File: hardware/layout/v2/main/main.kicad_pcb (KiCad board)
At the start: 4 copper layers, 31.5 x 76.5 mm, 52 parts, among them J1 KNX bus terminal pins, J2 AUX, J3 DALI, J4 Controller cable, J5 Interface DALI, J6 Interface logic, Q1 MJD45H11, Q2 BC857, U1 NCN5130MNTWG, U2 SCT2400TVBR, U3 REM3-2415S/A/CTRL 24V->15V 3W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, U4 TLP383, Y1 16MHz

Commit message: Updated DALI DC-DC converter from RECOM REM3-2415S/A to REC3-2415SRW/H2/A series across all variants, changed V3 OLED from 14-pin 0.5mm ZIF to 14-pin 0.62mm solder-tail FPC connector, and expanded assembly documentation with Mouser/Digi-Key/TME part numbers and alternative suppliers
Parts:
- U3: value REM3-2415S/A/CTRL 24V->15V 3W iso -> REC3-2415SRW/H2/A/CTRL 24V->15V 3W iso

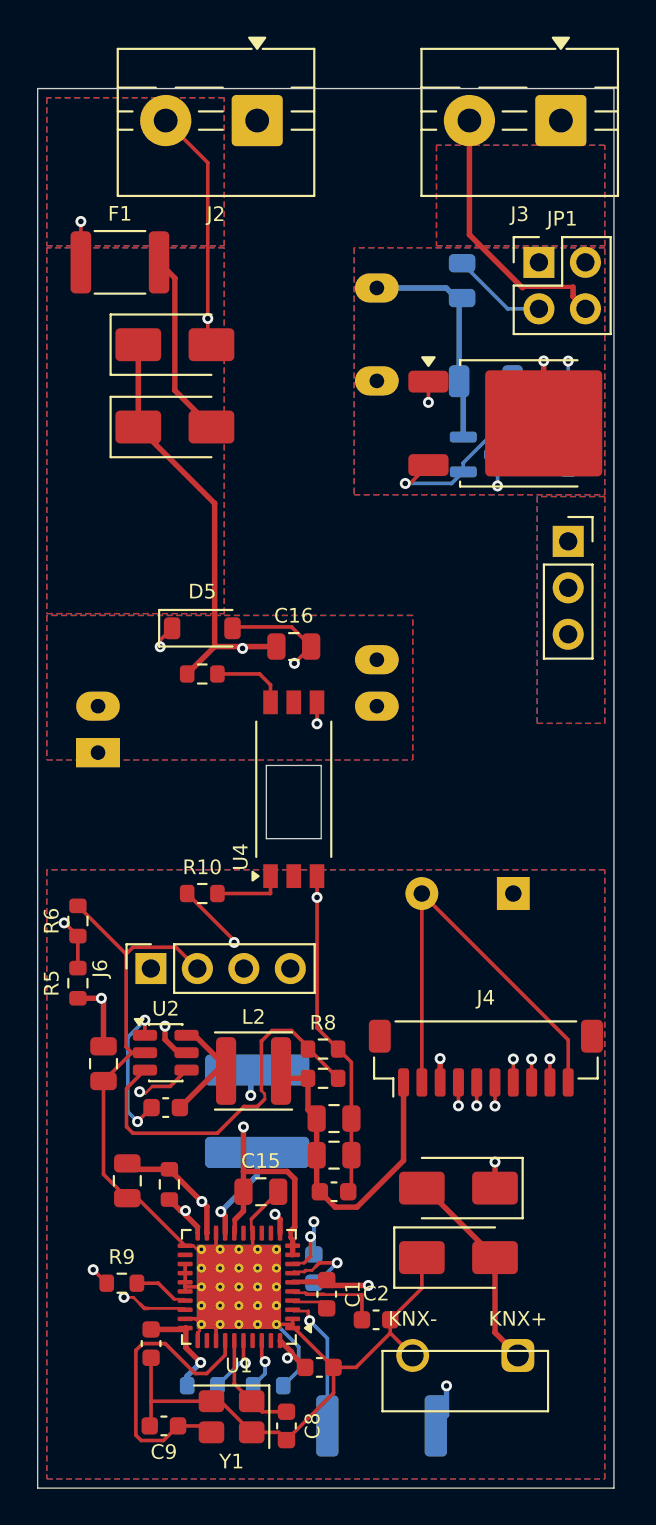
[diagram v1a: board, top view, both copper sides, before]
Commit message: Removed V1 hardware variant from CI workflows, updated AGENTS.md documentation to reflect V2/V3-only support
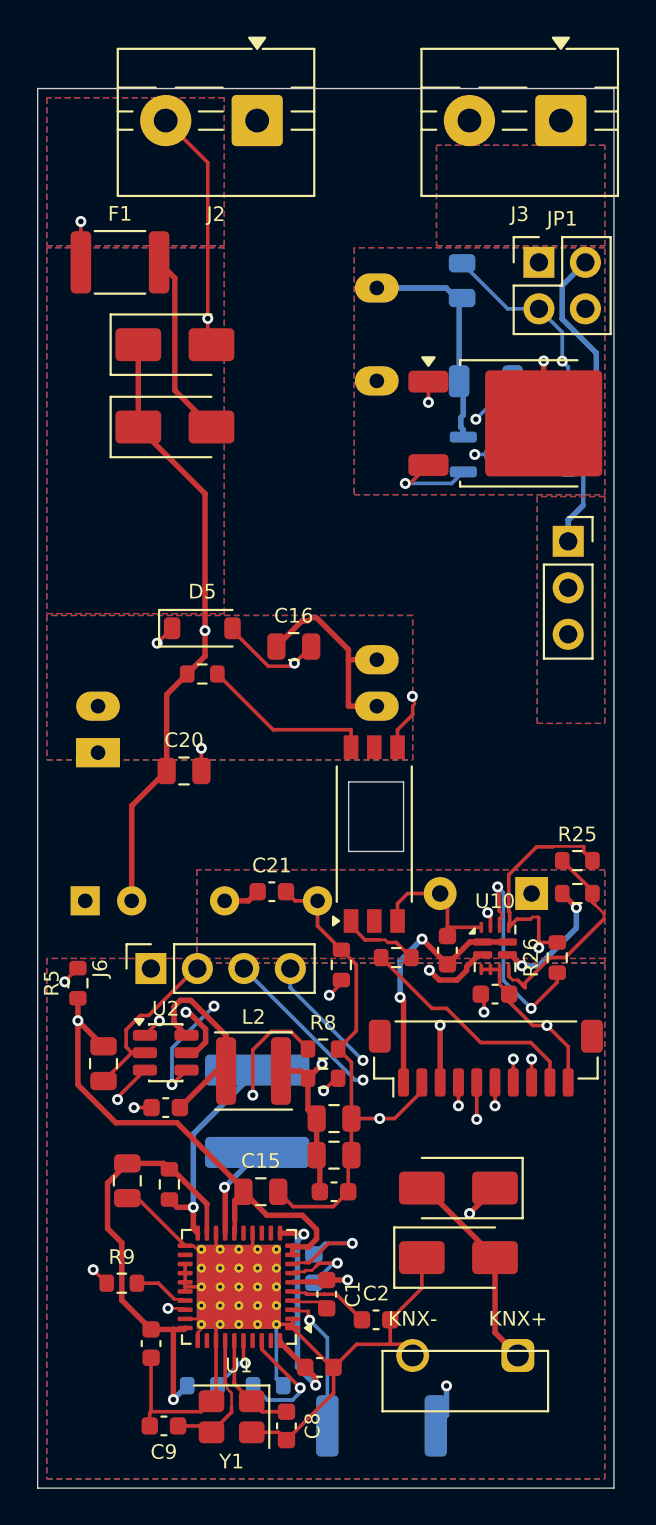
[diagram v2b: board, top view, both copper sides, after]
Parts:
- added C20: 10u 50V, Capacitor_SMD:C_0805_2012Metric, F.Cu at (8.00, -39.2)
- added C21: 10u 10V, Capacitor_SMD:C_0603_1608Metric, F.Cu at (12.8, -32.6)
- added C22: 100n 50V, Capacitor_SMD:C_0603_1608Metric, F.Cu at (25.0, -27.0)
- added C23: 10u 10V, Capacitor_SMD:C_0603_1608Metric, F.Cu at (22.4, -29.4)
- added R24: 30k, Resistor_SMD:R_0603_1608Metric, F.Cu at (29.5, -32.5)
- added R25: 10k, Resistor_SMD:R_0603_1608Metric, F.Cu at (29.5, -34.3)
- added R26: 100k 1%, Resistor_SMD:R_0603_1608Metric, F.Cu at (28.4, -29.0)
- added U10: TPS2121RUXR, Package_DFN_QFN:Texas_VQFN-HR-12_2x2.5mm_P0.5mm, F.Cu at (25.0, -29.5)
- added U9: TMR 1-2411 24V->5V 1W iso, gateway_fp:Converter_DCDC_TRACO_TMR1_SIP6, B.Cu at (2.60, -32.1)
- R5: value 120k 1% -> 100k 1%
- moved R6 14.6 mm to (16.6, -28.6)
- moved R10 11.2 mm to (19.6, -29.0)
- moved U4 5.04 mm to (18.4, -35.8)
- moved C4 1.00 mm to (27.0, -32.5)
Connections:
- C12 pad 1: +5V -> +5V_BUCK
- C13 pad 1: +5V -> +5V_BUCK
- C14 pad 1: +5V -> +5V_BUCK
- L2 pad 2: +5V -> +5V_BUCK
- R7 pad 1: +5V -> +5V_BUCK
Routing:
- net +5V_AUX: track 0.00 -> 30.3 mm, vias 0 -> 2
- net GND: track 158.7 -> 180.3 mm, vias 1 -> 3
- net GNDA: track 50.2 -> 71.5 mm, vias 2 -> 3
- net +5V_BUCK: track 0.00 -> 21.2 mm, vias 0 -> 2
- net AUX_P: track 35.5 -> 55.1 mm
- net VFILT: track 57.4 -> 74.0 mm, vias 3 -> 2
- net DALI_SUPPLY_OFF: track 25.1 -> 12.7 mm, vias 2 -> 0
- net N$11: track 0.00 -> 12.3 mm, vias 0 -> 2
- net CORE_PR1: track 0.00 -> 11.7 mm
- net +3V3_TRX: track 35.0 -> 46.1 mm, vias 4 -> 3
- net KNX_TXD: track 34.7 -> 24.0 mm
- net XTAL2: track 16.3 -> 7.58 mm
- net N$12: track 0.00 -> 7.44 mm, vias 0 -> 2
- net N$1: track 16.9 -> 23.3 mm, vias 2 -> 4
- net N$7: track 4.10 -> 9.52 mm
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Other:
- outline, holes or cut-outs redrawn

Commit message: Updated AUX-to-core converter from 1W TMR 1-2411 to 2W TMR 2411 (v3) and 3W TRN 3-2411 (v2) to handle WiFi TX peaks without KNX handover, relocated v3 converter to front protrusion tongue with AUX feed corridor along board edges, increased core hold-up capacitor C23 to 100µF 1206, added board slot between TRN3 pins 2/3 for creepage, updated domain regions and copper keepouts for new layouts, and added DCDC_SIP5/DCDC_SIP8_REMOTE symbols with converter parameter support in core_power.build()
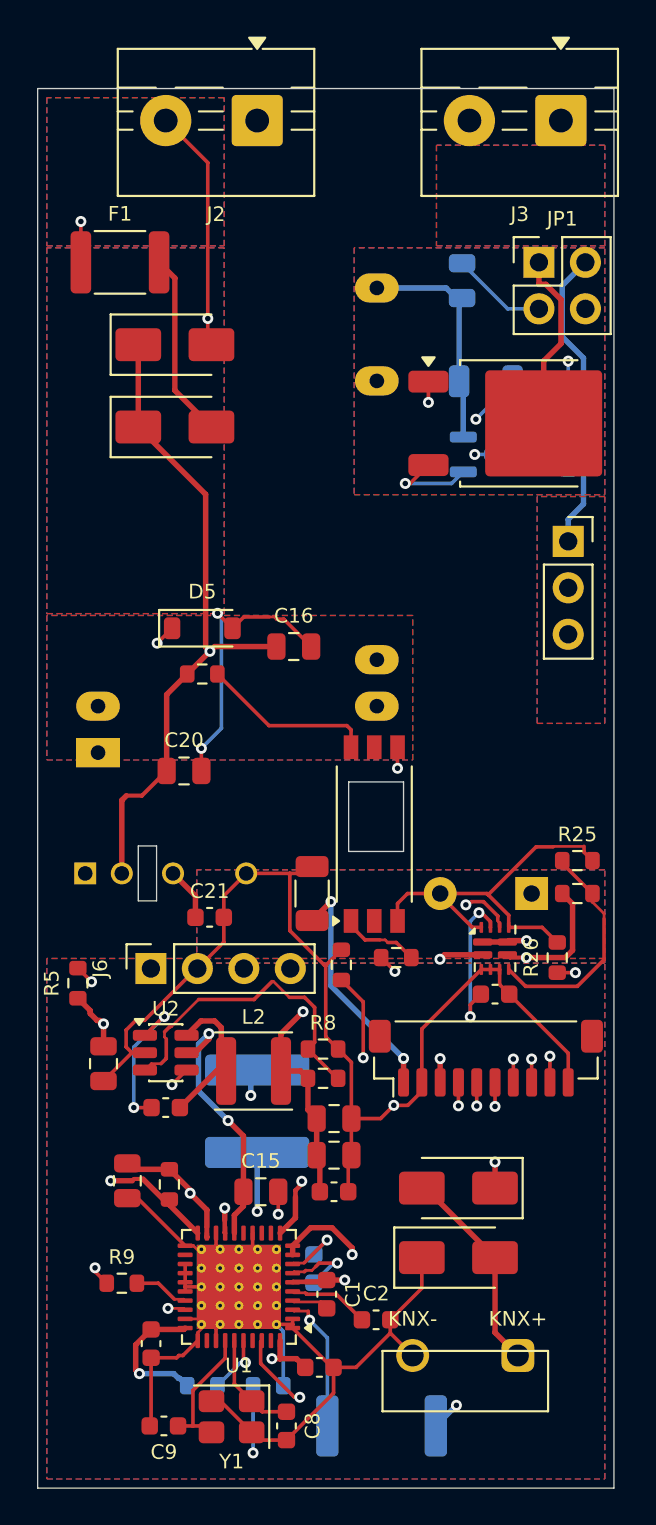
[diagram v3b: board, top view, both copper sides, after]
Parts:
- C23: value 10u 10V -> 100u 6.3V; footprint Capacitor_SMD:C_0603_1608Metric -> Capacitor_SMD:C_1206_3216Metric
- U9: value TMR 1-2411 24V->5V 1W iso -> TRN 3-2411 24V->5V 3W iso; footprint gateway_fp:Converter_DCDC_TRACO_TMR1_SIP6 -> gateway_fp:Converter_DCDC_TRACO_TRN3_SIP5
- moved C23 8.02 mm to (15.0, -32.5)
- moved C21 3.68 mm to (9.40, -31.2)
- moved U9 1.50 mm to (2.60, -33.6)
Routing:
- net +5V: track 14.2 -> 27.0 mm, vias 2 -> 3
- net KNX_RXD: track 40.8 -> 28.0 mm
- net GNDA: track 71.5 -> 62.4 mm
- net +5V_BUCK: track 21.2 -> 28.1 mm
- net VDD1M: track 11.9 -> 17.3 mm, vias 1 -> 2
- net FANIN: track 6.77 -> 12.0 mm, vias 1 -> 2
- net N$3: track 22.6 -> 17.6 mm, vias 3 -> 0
- net AUX_P: track 55.1 -> 50.2 mm
- net VFILT: track 74.0 -> 78.5 mm, vias 2 -> 4
- net +3V3: track 23.9 -> 19.4 mm
- net DALI_RX: track 20.2 -> 16.5 mm, vias 2 -> 1
- net N$11: track 12.3 -> 15.4 mm
- net SW: track 10.9 -> 8.10 mm
- net KNX_TXD: track 24.0 -> 26.8 mm
- net CEQ2: track 6.09 -> 3.51 mm
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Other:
- outline, holes or cut-outs redrawn
